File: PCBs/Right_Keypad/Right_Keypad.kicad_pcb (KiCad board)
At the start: 4 copper layers, 86.4 x 106.8 mm, 59 parts, among them J1 Conn_Right_Keypad, Q1 NPN, Q2 NPN, Q3 NPN, SW1 SW_Push, SW10 SW_Push, SW11 SW_Push, SW12 SW_Push, SW13 SW_Push, SW14 SW_Push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

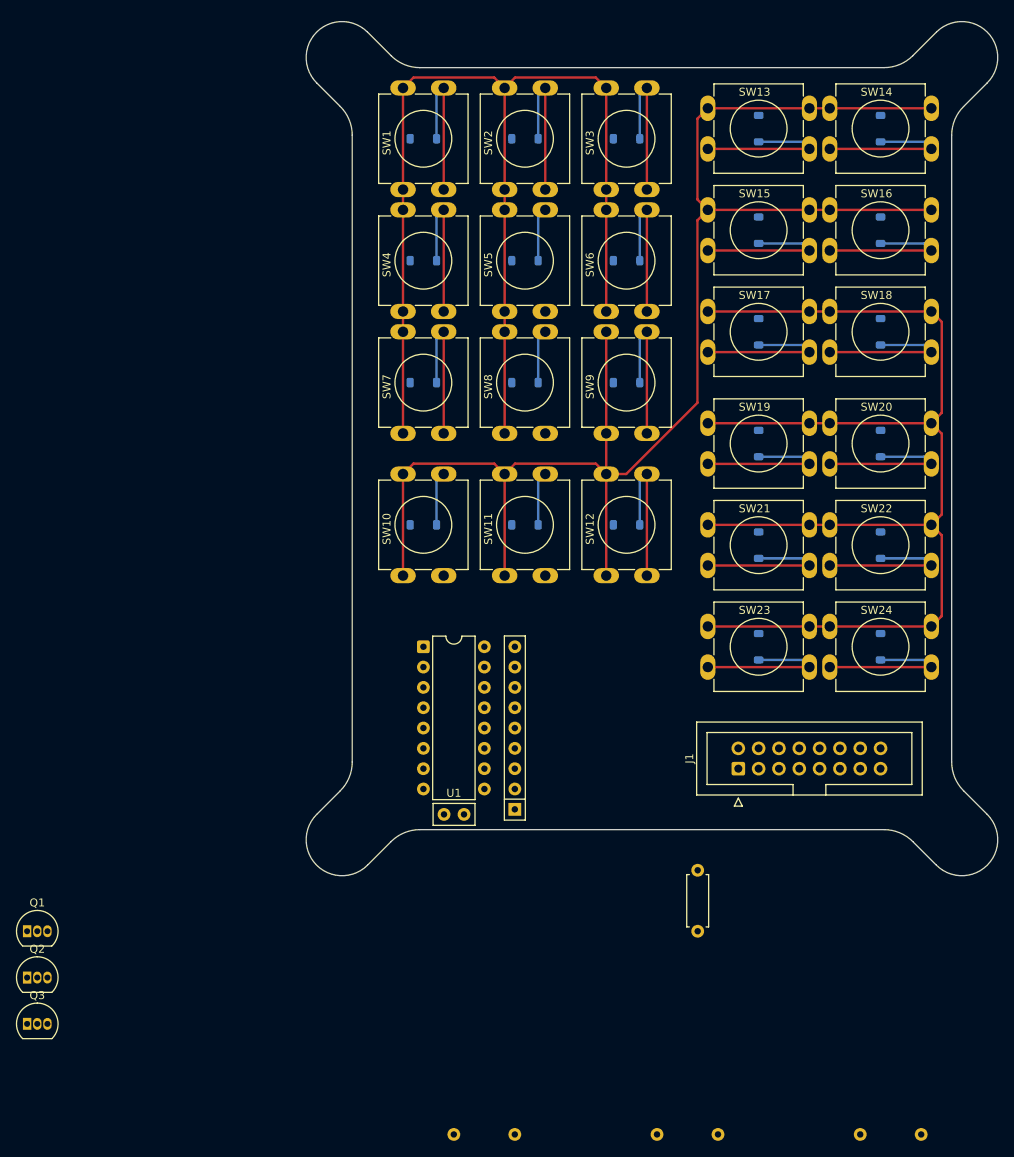
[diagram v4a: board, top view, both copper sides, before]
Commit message: UART+RS485 + KiCad 10 + keypad PCB v1
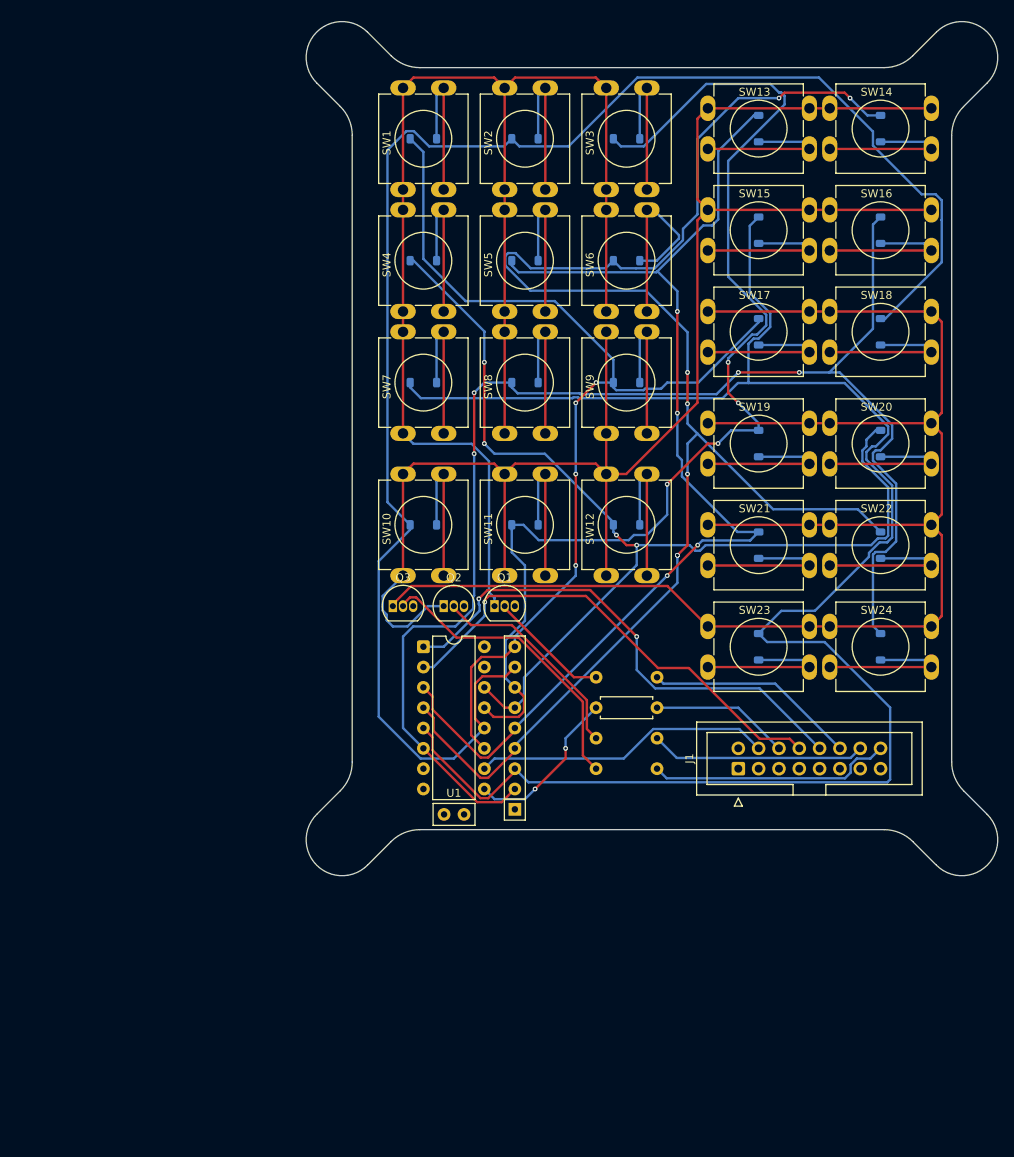
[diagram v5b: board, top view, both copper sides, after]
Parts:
- moved Q1 71.2 mm to (115.6, 118.1)
- moved Q2 69.8 mm to (109.2, 118.1)
- moved Q3 69.4 mm to (102.9, 118.1)
- moved R2 66.0 mm to (135.9, 127.0)
- moved R3 50.1 mm to (135.9, 134.6)
- moved R4 49.1 mm to (135.9, 138.4)
- moved R1 20.9 mm to (135.9, 130.8), turned to 180 degrees
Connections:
- J1 pad 4: Net-(J1-IN_DFM) -> unconnected-(J1-PIN_4-Pad4)
- U1 pad 10: Net-(J1-IN_DFM) -> unconnected-(U1-DS-Pad10)
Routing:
- net Net-(D15-A): track 0.00 -> 221.1 mm
- net Net-(D10-A): track 0.00 -> 203.5 mm
- net Net-(D14-A): track 0.00 -> 200.4 mm, vias 0 -> 7
- net Net-(D16-A): track 0.00 -> 177.8 mm, vias 0 -> 4
- net Net-(D11-A): track 0.00 -> 148.1 mm, vias 0 -> 4
- net Net-(D13-A): track 0.00 -> 142.7 mm, vias 0 -> 4
- net Net-(D12-A): track 0.00 -> 131.8 mm, vias 0 -> 4
- net Net-(D1-A): track 0.00 -> 127.1 mm, vias 0 -> 4
- net Net-(J1-IN_PL): track 0.00 -> 64.1 mm, vias 0 -> 2
- net Net-(J1-IN_CP): track 0.00 -> 59.7 mm, vias 0 -> 1
- net Net-(Q3-C): track 154.4 -> 197.2 mm
- net Net-(Q3-B): track 0.00 -> 37.5 mm
- net (no net): track 0.00 -> 37.3 mm
- net Net-(Q1-C): track 141.9 -> 172.4 mm
- net Net-(J1-ROW_3): track 0.00 -> 30.6 mm
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
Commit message: ESD protection and stuff
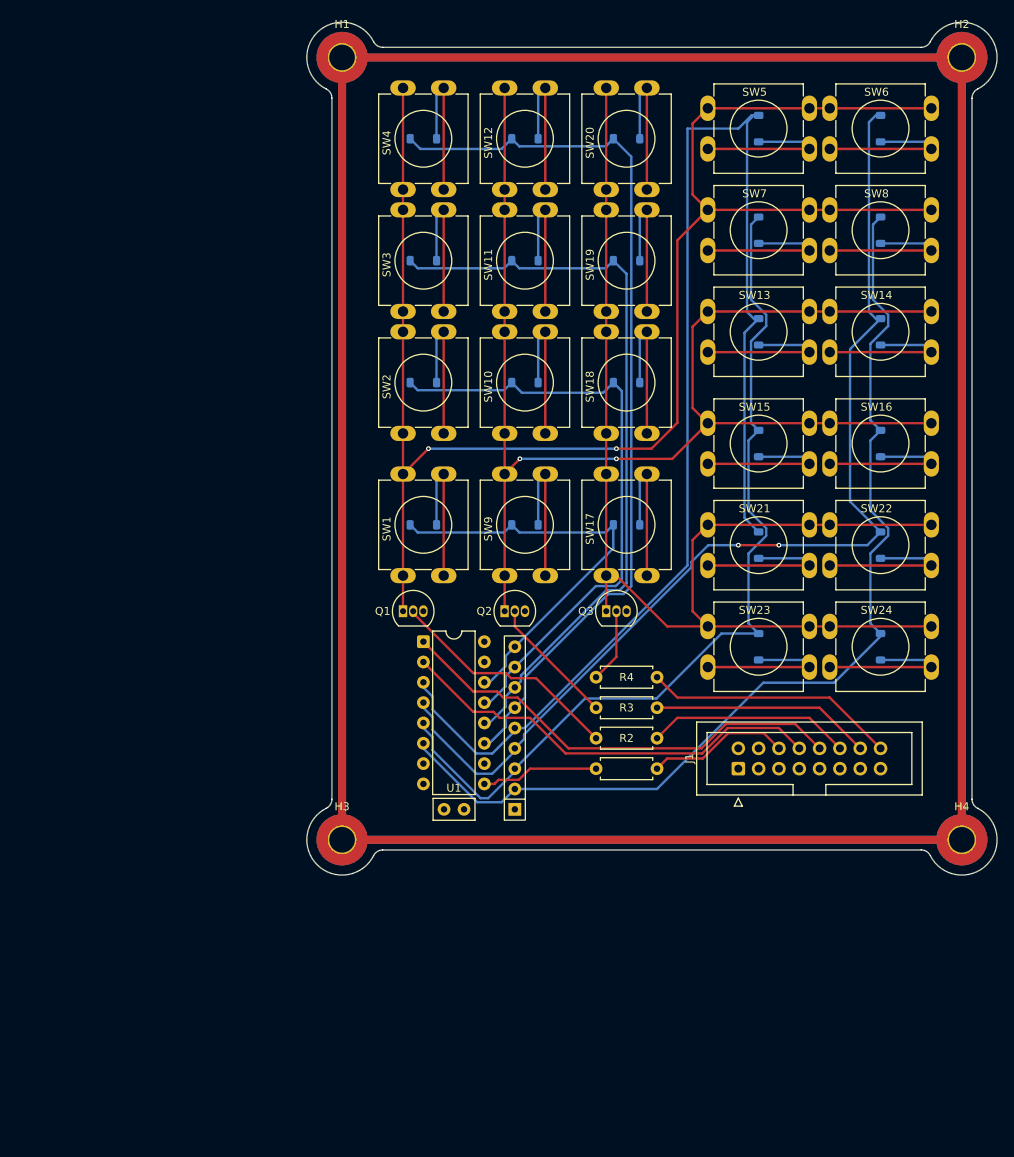
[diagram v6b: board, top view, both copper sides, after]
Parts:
- added H1: MountingHole_Pad, MountingHole:MountingHole_3.2mm_M3_Pad_TopBottom, F.Cu at (96.5, 49.5)
- added H2: MountingHole_Pad, MountingHole:MountingHole_3.2mm_M3_Pad_TopBottom, F.Cu at (174.0, 49.5)
- added H3: MountingHole_Pad, MountingHole:MountingHole_3.2mm_M3_Pad_TopBottom, F.Cu at (96.5, 147.3)
- added H4: MountingHole_Pad, MountingHole:MountingHole_3.2mm_M3_Pad_TopBottom, F.Cu at (174.0, 147.3)
- R2, R3, R4: moved to F.Cu
- moved D12 49.9 mm to (119.4, 59.7)
- moved SW12 49.9 mm to (116.8, 66.0)
- moved D20 49.6 mm to (132.1, 59.7), turned to 180 degrees
- moved SW8 49.3 mm to (157.5, 68.6), turned to 0 degrees
- moved D8 48.4 mm to (163.8, 71.1), turned to 90 degrees
- moved D1 48.3 mm to (106.7, 108.0)
- moved SW1 48.3 mm to (104.1, 114.3)
- moved SW7 47.2 mm to (142.2, 68.6), turned to 0 degrees
- moved D7 46.0 mm to (148.6, 71.1), turned to 90 degrees
- moved SW20 40.4 mm to (129.5, 66.0), turned to 90 degrees
- moved SW6 37.8 mm to (157.5, 55.9), turned to 0 degrees
- moved SW5 35.9 mm to (142.2, 55.9), turned to 0 degrees
- moved D6 35.8 mm to (163.8, 58.4), turned to 90 degrees
- moved SW17 35.4 mm to (129.5, 114.3), turned to 90 degrees
- moved D5 33.6 mm to (148.6, 58.4), turned to 90 degrees
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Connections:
- U1 pad 11: Net-(D1-A) -> Net-(D12-A)
- U1 pad 12: Net-(D10-A) -> Net-(D11-A)
- U1 pad 13: Net-(D11-A) -> Net-(D10-A)
- U1 pad 14: Net-(D12-A) -> Net-(D1-A)
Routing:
- net Chassis: track 0.00 -> 701.0 mm
- net Net-(D10-A): track 203.5 -> 76.9 mm
- net Net-(D15-A): track 221.1 -> 112.5 mm
- net Net-(D1-A): track 127.1 -> 54.0 mm, vias 4 -> 0
- net Net-(D14-A): track 200.4 -> 132.1 mm, vias 7 -> 2
- net Net-(D11-A): track 148.1 -> 94.4 mm, vias 4 -> 0
- net Net-(D16-A): track 177.8 -> 126.4 mm, vias 4 -> 0
- net Net-(Q3-E): track 197.2 -> 152.1 mm
- net Net-(Q2-C): track 208.2 -> 165.5 mm, vias 0 -> 2
- net (no net): track 37.3 -> 0.00 mm
- net Net-(Q1-B): track 172.4 -> 202.7 mm, vias 0 -> 2
- net Net-(Q3-C): track 37.5 -> 9.31 mm
- net Net-(D13-A): track 142.7 -> 167.0 mm, vias 4 -> 0
- net Net-(D12-A): track 131.8 -> 113.1 mm, vias 4 -> 0
- net Net-(Q1-E): track 15.2 -> 30.2 mm
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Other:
- board size 86.4 x 106.8 mm -> 86.3 x 106.6 mm

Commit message: stuff
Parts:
- moved RN1 0.64 mm to (118.1, 142.9)
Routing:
- net Net-(U1-Q7): track 15.0 -> 15.7 mm
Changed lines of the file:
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@@
 	(footprint "Resistor_THT:R_Array_SIP9"
 		(layer "F.Cu")
-		(at 118.115 143.51 90)
+		(at 118.11 142.875 90)
 		(descr "9-pin Resistor SIP pack")
 		(tags "R")
@@
 	)
 	(segment
-		(start 114.94 140.335)
-		(end 115.57 140.335)
+		(start 118.745 139.065)
+		(end 119.38 138.43)
 		(width 0.3)
 		(layer "F.Cu")
@@
 	)
 	(segment
-		(start 116.085 139.82)
-		(end 118.625 139.82)
+		(start 115.575 139.065)
+		(end 118.745 139.065)
 		(width 0.3)
 		(layer "F.Cu")
@@
 	)
 	(segment
-		(start 118.625 139.82)
-		(end 120.015 138.43)
+		(start 114.305 140.97)
+		(end 114.94 140.335)
 		(width 0.3)
 		(layer "F.Cu")
@@
 	)
 	(segment
-		(start 120.015 138.43)
+		(start 119.38 138.43)
 		(end 128.27 138.43)
 		(width 0.3)
@@
 	)
 	(segment
-		(start 114.305 140.97)
-		(end 114.94 140.335)
-		(width 0.3)
-		(layer "F.Cu")
-		(net "Net-(U1-Q7)")
-	)
-	(segment
-		(start 115.57 140.335)
-		(end 116.085 139.82)
+		(start 114.305 140.335)
+		(end 115.575 139.065)
 		(width 0.3)
 		(layer "F.Cu")
@@
 	)
 	(segment
-		(start 116.664327 129.54)
-		(end 118.471346 129.54)
-		(width 0.3)
-		(layer "F.Cu")
-		(net "Net-(J1-IN_PL)")
-	)
-	(segment
-		(start 141.460788 135.89)
-		(end 144.500788 132.85)
-		(width 0.3)
-		(layer "F.Cu")
-		(net "Net-(J1-IN_PL)")
-	)
-	(segment
-		(start 144.500788 132.85)
-		(end 153.17 132.85)
+		(start 113.035 128.905)
+		(end 118.745 128.905)
 		(width 0.3)
 		(layer "F.Cu")
@@
 	)
 	(segment
-		(start 118.471346 129.54)
-		(end 124.821346 135.89)
+		(start 125.73 135.89)
+		(end 141.460788 135.89)
 		(width 0.3)
 		(layer "F.Cu")
@@
 	)
 	(segment
-		(start 112.915 128.785)
-		(end 115.909327 128.785)
+		(start 106.685 122.555)
+		(end 113.035 128.905)
 		(width 0.3)
 		(layer "F.Cu")
@@
 	)
 	(segment
-		(start 106.685 122.555)
-		(end 112.915 128.785)
+		(start 144.500788 132.85)
+		(end 153.17 132.85)
 		(width 0.3)
 		(layer "F.Cu")
@@
 	)
 	(segment
-		(start 124.821346 135.89)
-		(end 141.460788 135.89)
+		(start 141.460788 135.89)
+		(end 144.500788 132.85)
 		(width 0.3)
 		(layer "F.Cu")
@@
 	)
 	(segment
-		(start 115.909327 128.785)
-		(end 116.664327 129.54)
+		(start 118.745 128.905)
+		(end 125.73 135.89)
 		(width 0.3)
 		(layer "F.Cu")
@@
 	)
 	(segment
-		(start 115.45 131.325)
-		(end 116.205 132.08)
-		(width 0.3)
-		(layer "F.Cu")
-		(net "Net-(J1-IN_CP)")
-	)
-	(segment
-		(start 116.205 132.08)
-		(end 120.015 132.08)
-		(width 0.3)
-		(layer "F.Cu")
-		(net "Net-(J1-IN_CP)")
-	)
-	(segment
 		(start 141.532894 136.525)
 		(end 144.707894 133.35)
@@
 	)
 	(segment
-		(start 120.015 132.08)
-		(end 124.46 136.525)
+		(start 151.13 133.35)
+		(end 153.67 135.89)
 		(width 0.3)
 		(layer "F.Cu")
@@
 	)
 	(segment
-		(start 144.707894 133.35)
-		(end 151.13 133.35)
+		(start 123.825 136.525)
+		(end 141.532894 136.525)
 		(width 0.3)
 		(layer "F.Cu")
@@
 	)
 	(segment
-		(start 112.915 131.325)
-		(end 115.45 131.325)
+		(start 118.745 131.445)
+		(end 123.825 136.525)
 		(width 0.3)
 		(layer "F.Cu")
@@
 	)
 	(segment
-		(start 124.46 136.525)
-		(end 141.532894 136.525)
+		(start 144.707894 133.35)
+		(end 151.13 133.35)
 		(width 0.3)
 		(layer "F.Cu")
@@
 	)
 	(segment
-		(start 151.13 133.35)
-		(end 153.67 135.89)
+		(start 113.035 131.445)
+		(end 118.745 131.445)
 		(width 0.3)
 		(layer "F.Cu")
@@
 	(segment
 		(start 106.685 125.095)
-		(end 112.915 131.325)
+		(end 113.035 131.445)
 		(width 0.3)
 		(layer "F.Cu")
@@
 	)
 	(segment
-		(start 120.77 127.12)
+		(start 127 134.62)
 		(end 128.27 134.62)
 		(width 0.3)
@@
 	)
 	(segment
-		(start 105.41 118.745)
-		(end 105.41 118.97)
+		(start 118.745 126.365)
+		(end 127 134.62)
 		(width 0.3)
 		(layer "F.Cu")
@@
 	)
 	(segment
-		(start 117.638654 127.12)
-		(end 120.77 127.12)
+		(start 112.805 126.365)
+		(end 118.745 126.365)
 		(width 0.3)
 		(layer "F.Cu")
@@
 	)
 	(segment
-		(start 112.925 126.485)
-		(end 117.003654 126.485)
-		(width 0.3)
-		(layer "F.Cu")
-		(net "Net-(Q1-E)")
-	)
-	(segment
-		(start 117.003654 126.485)
-		(end 117.638654 127.12)
+		(start 105.41 118.745)
+		(end 105.41 118.97)
 		(width 0.3)
 		(layer "F.Cu")
@@
 	(segment
 		(start 105.41 118.97)
-		(end 112.925 126.485)
+		(end 112.805 126.365)
 		(width 0.3)
 		(layer "F.Cu")

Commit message: finishing touches and silkscreen stuff
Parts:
- H1, H2, H3, H4: footprint MountingHole:MountingHole_3.2mm_M3_Pad_TopBottom -> MountingHole:MountingHole_3.2mm_M3_Pad
- moved Q3 1.27 mm to (130.8, 118.7)
- moved Q1 1.27 mm to (105.4, 118.7)
- moved Q2 1.27 mm to (118.1, 118.7)
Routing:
- net Net-(D13-A): track 167.0 -> 113.8 mm
- net Net-(Q1-B): track 202.7 -> 205.4 mm, vias 2 -> 1
- net Net-(Q2-C): track 165.5 -> 168.1 mm, vias 2 -> 1
- net Net-(D14-A): track 132.1 -> 134.0 mm
- net Net-(Q2-B): track 16.3 -> 17.2 mm
- net Net-(Q3-E): track 152.1 -> 152.9 mm
- net Net-(D12-A): track 113.1 -> 112.5 mm
- net Net-(Q3-C): track 9.31 -> 9.83 mm
- net Net-(Q1-E): track 30.2 -> 29.7 mm
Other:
- board text added: "01"
- board text added: "02"
- board text added: "03"
- board text added: "04"
- board text added: "05"
- board text added: "06"
- board text added: "07"
- board text added: "08"
- board text added: "09"
- board text added: "10"
- board text added: "11"
- board text added: "12"
- board text added: "13"
- board text added: "14"
- board text added: "15"
- board text added: "16"
- board text added: "17"
- board text added: "18"
- board text added: "19"
- board text added: "20"
- board text added: "21"
- board text added: "22"
- board text added: "23"
- board text added: "24"
